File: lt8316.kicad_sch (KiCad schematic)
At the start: 17 parts

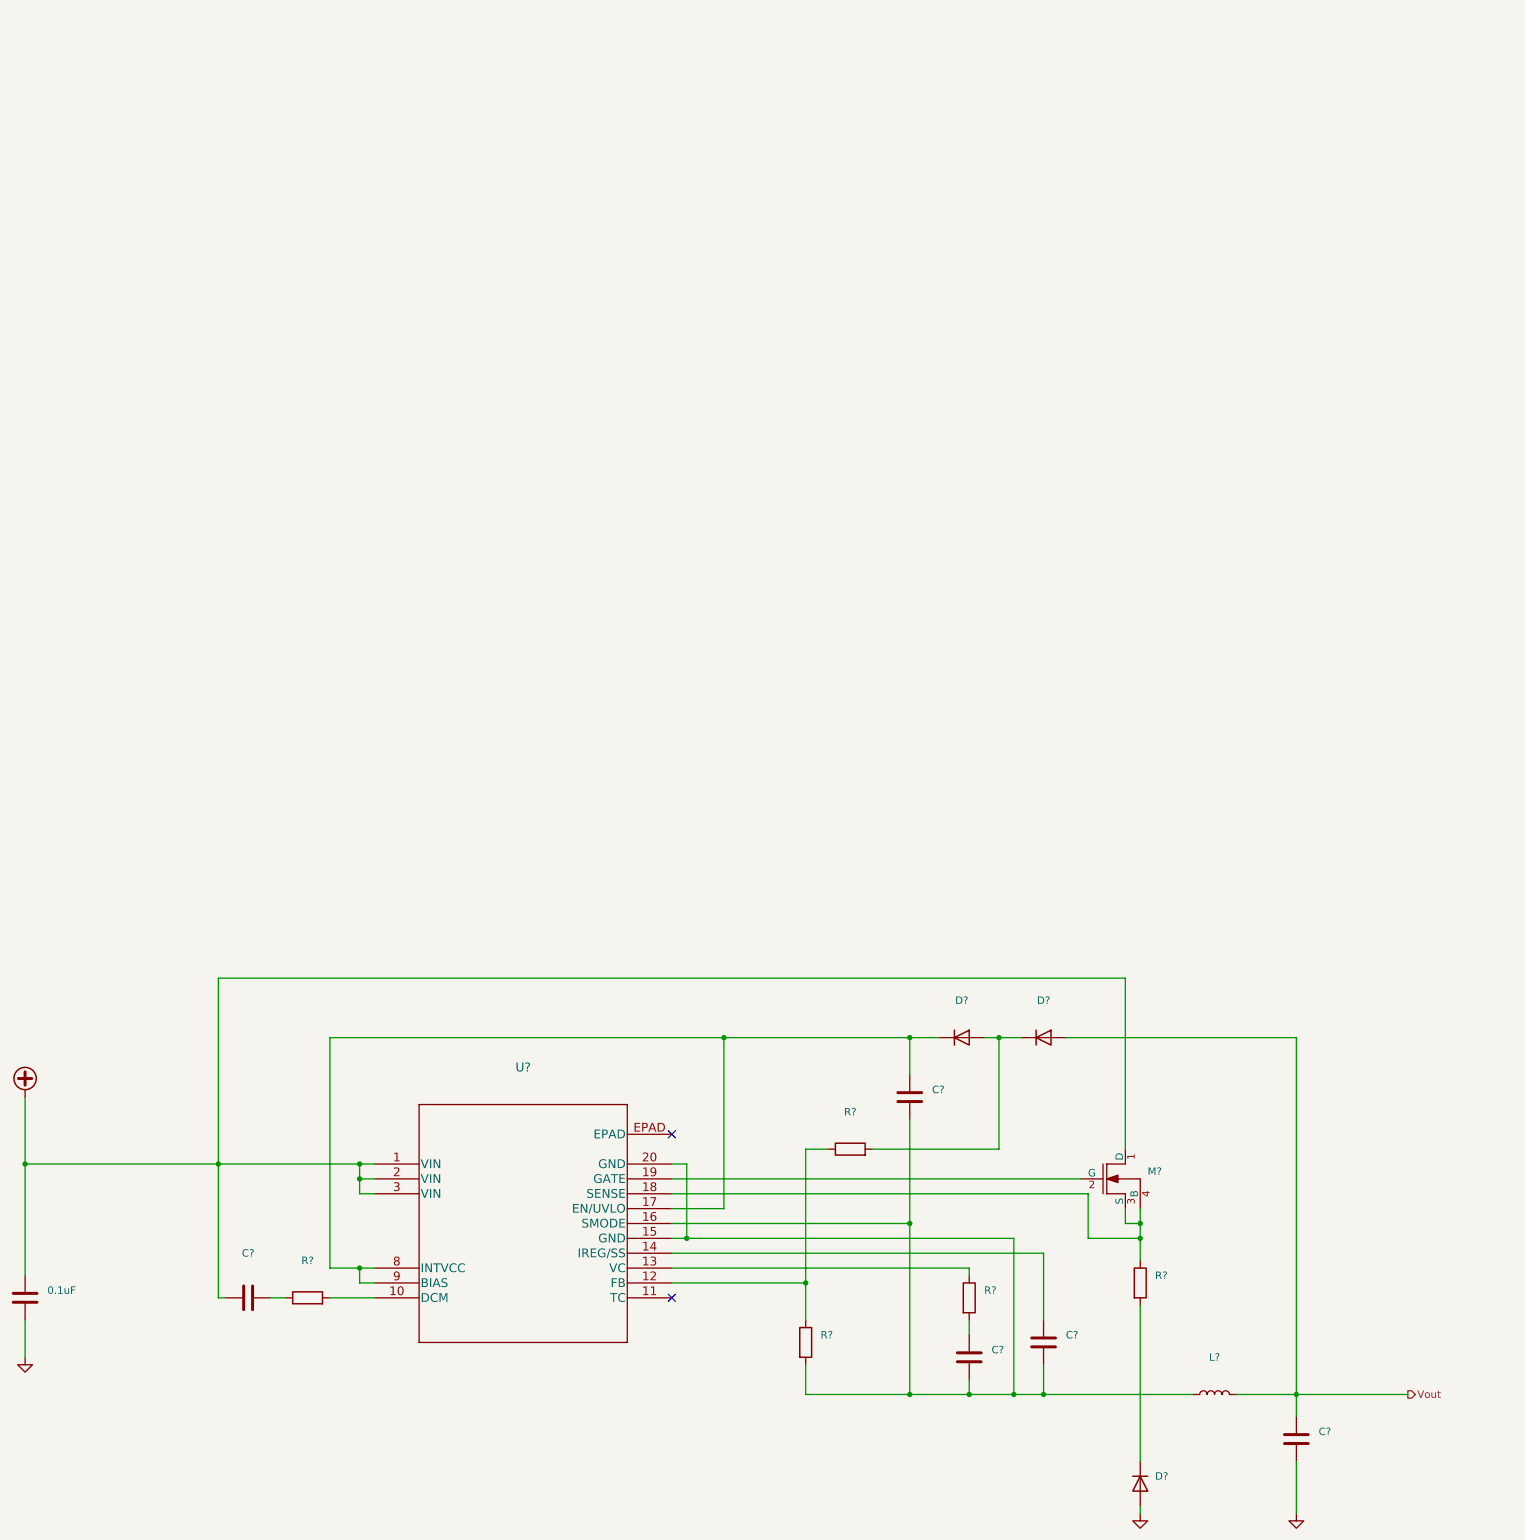
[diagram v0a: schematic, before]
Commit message: change scheme of LT8316EFE and change mosfet symbol
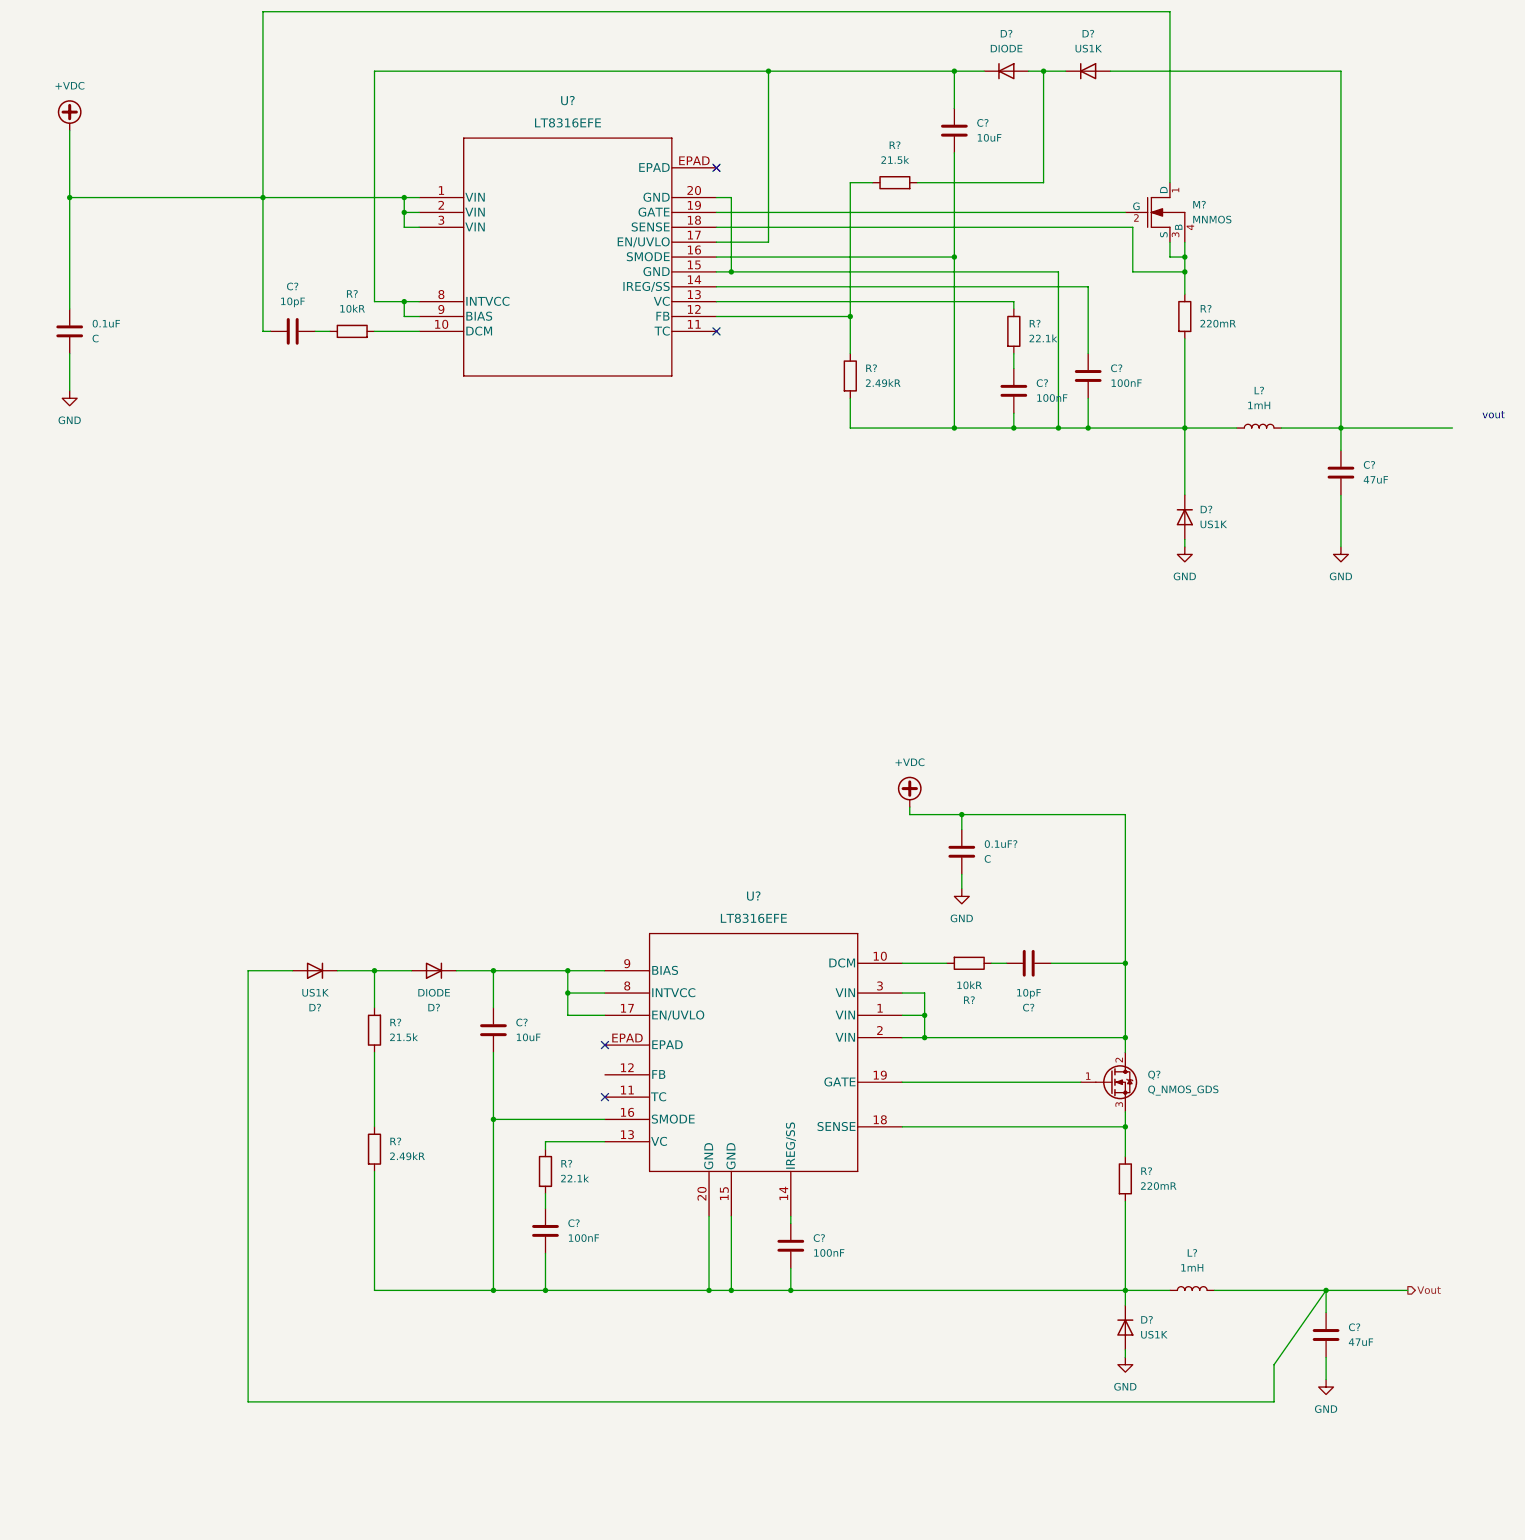
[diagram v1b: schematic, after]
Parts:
- added 0.1uF?: C, symbol Device:C
- added C?: 10pF, symbol Device:C
- added C?: 10uF, symbol Device:C
- added C?: 47uF, symbol Device:C
- added C? (x2): 100nF, symbol Device:C
- added D? (x2): US1K, Diode_SMD:D_SMA, symbol Diode:US1K
- added D?: DIODE, symbol Simulation_SPICE:DIODE
- added L?: 1mH, symbol Device:L
- added Q?: Q_NMOS_GDS, symbol Device:Q_NMOS_GDS
- added R?: 21.5k, symbol Device:R
- added R?: 220mR, symbol Device:R
- added R?: 2.49kR, symbol Device:R
- added R?: 10kR, symbol Device:R
- added R?: 22.1k, symbol Device:R
- added U?: LT8316EFE, TSSOP20_FE_BB_16_, symbol Library_indicator:LT8316EFE
- 0.1uF: value (none) -> C
- C?: value (none) -> 47uF
- C? (x2): value (none) -> 100nF
- C?: value (none) -> 10pF
- C?: value (none) -> 10uF
- D? (x2): value (none) -> US1K; footprint (none) -> Diode_SMD:D_SMA
- D?: value (none) -> DIODE
- L?: value (none) -> 1mH
- M?: value (none) -> MNMOS
- R?: value (none) -> 2.49kR
- R?: value (none) -> 22.1k
- R?: value (none) -> 10kR
- R?: value (none) -> 220mR
- R?: value (none) -> 21.5k
- U?: value (none) -> LT8316EFE; footprint (none) -> TSSOP20_FE_BB_16_
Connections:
- net +VDC: now also 0.1uF?.1, C?.1, Q?.2 (D), U?.1 (VIN), U?.2 (VIN), U?.3 (VIN)
- net GND: now also 0.1uF?.2, C?.2, D?.2 (A)
- net Vout: now also C?.1, D?.2 (A), L?.2; no longer C?.1, D?.2 (A), L?.2
- net at C?.2, C?.2, C?.2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: now also D?.1 (K), R?.2
- new net: R?.1, R?.1
- new net: D?.1 (A), D?.1 (K), R?.2
- new net: C?.1, D?.2 (A), L?.2
- new net: Q?.3 (S), R?.1, U?.18 (SENSE)
- new net: C?.2, C?.2, C?.2, D?.1 (K), L?.1, R?.2, R?.2, U?.15 (GND), U?.16 (SMODE), U?.20 (GND)
- new net: C?.2, R?.1
- new net: R?.2, U?.10 (DCM)
- new net: R?.1, U?.13 (VC)
- new net: C?.1, U?.14 (IREG/SS)
- new net: C?.1, D?.2 (K), U?.17 (EN/UVLO), U?.8 (INTVCC), U?.9 (BIAS)
- new net: Q?.1 (G), U?.19 (GATE)
- new net: C?.1, R?.2
- no-connect marks 2 -> 4
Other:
- note added: "vout"
- moved on the sheet: 0.1uF, C?, D?, L?, M?, R?, U?
